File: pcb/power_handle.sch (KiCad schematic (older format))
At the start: 51 parts, among them J1 PJ-202A, J2 USB_C_Receptacle_USB2.0, Q1 PSMN6R0-25YLB, Q2 PSMN6R0-25YLB, Q3 BSS214NW, SW1 SW_SPST, U1 MCP73831T-2ATI/OT, U2 PAM2423, U3 BQ29703DSET

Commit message: pcb: Cleanup BOM items (#7)
Replaced out of stock components with substitutes
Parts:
- C10: Digikey 493-3094-1-ND -> 493-13738-1-ND
- D2, D4: Digikey B340LA-FDICT-ND -> 641-1258-1-ND
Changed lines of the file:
@@
 F 1 "B340LA-13-F" H 6200 3724 50  0000 C CNN
 F 2 "Diode_SMD:D_SMA" H 6200 3675 50  0001 C CNN
-F 3 "https://www.diodes.com/assets/Datasheets/ds30240.pdf" H 6200 3850 50  0001 C CNN
-F 4 "B340LA-FDICT-ND" H 6200 3850 50  0001 C CNN "Digikey"
+F 3 "https://www.comchiptech.com/admin/files/product/CDBA340L-HF%20RevC514368.pdf" H 6200 3850 50  0001 C CNN
+F 4 "641-1258-1-ND" H 6200 3850 50  0001 C CNN "Digikey"
 	1    6200 3850
 	-1   0    0    1
@@
 F 1 "B340LA-13-F" H 10450 2724 50  0000 C CNN
 F 2 "Diode_SMD:D_SMA" H 10450 2675 50  0001 C CNN
-F 3 "https://www.diodes.com/assets/Datasheets/ds30240.pdf" H 10450 2850 50  0001 C CNN
-F 4 "B340LA-FDICT-ND" H 10450 2850 50  0001 C CNN "Digikey"
+F 3 "https://www.comchiptech.com/admin/files/product/CDBA340L-HF%20RevC514368.pdf" H 10450 2850 50  0001 C CNN
+F 4 "641-1258-1-ND" H 10450 2850 50  0001 C CNN "Digikey"
 	1    10450 2850
 	-1   0    0    1
@@
 F 1 "1000u" H 7715 3955 50  0000 L CNN
 F 2 "Capacitor_SMD:CP_Elec_10x12.6" H 7600 4000 50  0001 C CNN
-F 3 "https://www.nichicon.co.jp/english/products/pdfs/e-pcg.pdf" H 7600 4000 50  0001 C CNN
-F 4 "493-3094-1-ND" H 7600 4000 50  0001 C CNN "Digikey"
+F 3 "https://www.nichicon.co.jp/english/products/pdfs/e-pcr.pdf" H 7600 4000 50  0001 C CNN
+F 4 "493-13738-1-ND" H 7600 4000 50  0001 C CNN "Digikey"
 	1    7600 4000
 	1    0    0    -1

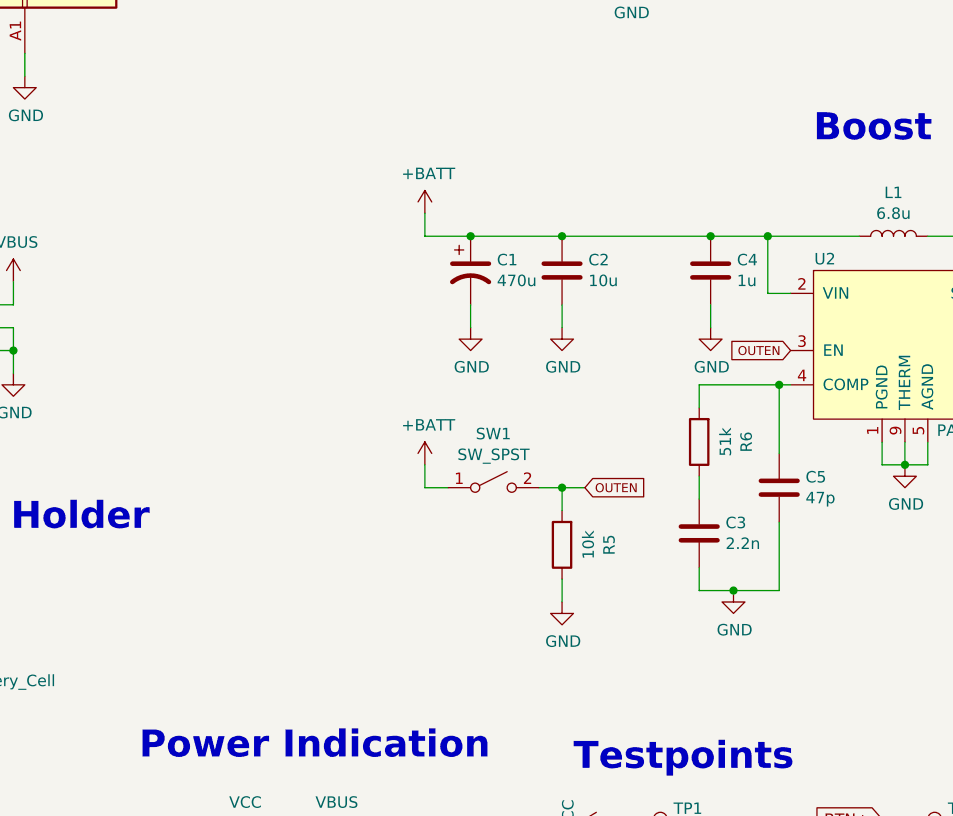
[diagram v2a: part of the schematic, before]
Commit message: pcb: implement improvements described in rev 1 bringup notes (#23)
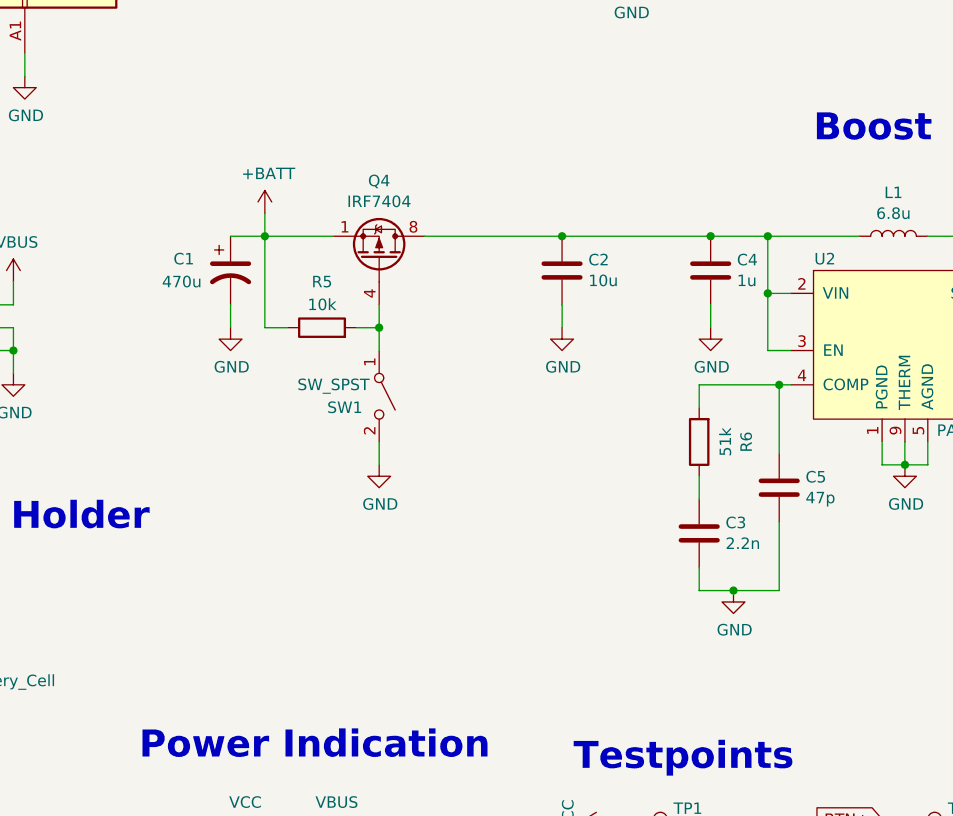
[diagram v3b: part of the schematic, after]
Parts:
- added Q4: IRF7404, Package_SO:SOIC-8_3.9x4.9mm_P1.27mm, symbol Transistor_FET:IRF7404
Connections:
- net +BATT: now also R5.1, Q4.1 (S), Q4.2 (S), Q4.3 (S); no longer C2.2, C4.2, L1.1, SW1.1 (A), U2.2 (VIN)
- net GND: now also SW1.2 (B); no longer R5.1
- removed net OUTEN: R5.2, SW1.2 (B), U2.3 (EN)
- new net: C2.2, C4.2, L1.1, Q4.5 (D), Q4.6 (D), Q4.7 (D), Q4.8 (D), U2.2 (VIN), U2.3 (EN)
- new net: Q4.4 (G), R5.2, SW1.1 (A)
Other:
- moved on the sheet: C1, R5, SW1
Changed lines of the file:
@@
 Connection ~ 6750 3850
-Wire Wire Line
-	3300 3750 3300 3850
-Wire Wire Line
-	3300 3850 3500 3850
-Wire Wire Line
-	3900 3850 3500 3850
-Connection ~ 3500 3850
 Wire Wire Line
 	3900 3850 4550 3850
@@
 Connection ~ 3900 3850
 Wire Wire Line
-	3500 4250 3500 4150
-Wire Wire Line
 	3900 4250 3900 4150
 Connection ~ 4550 3850
@@
 Wire Wire Line
 	4550 4250 4550 4150
-Text GLabel 4900 4350 0    39   Input ~ 0
-OUTEN
-Text GLabel 4000 4950 2    39   Input ~ 0
-OUTEN
-Wire Wire Line
-	4000 4950 3900 4950
-Wire Wire Line
-	3900 4950 3900 5050
-Wire Wire Line
-	3900 5350 3900 5450
-Wire Wire Line
-	3800 4950 3900 4950
-Connection ~ 3900 4950
-Wire Wire Line
-	3300 4850 3300 4950
-Wire Wire Line
-	3300 4950 3400 4950
+Wire Wire Line
+	3100 4750 3100 4850
 Wire Wire Line
 	4500 4900 4500 5000
@@
 $EndComp
 $Comp
-L power:+BATT #PWR012
-U 1 1 61903928
-P 3300 4850
-F 0 "#PWR012" H 3300 4700 50  0001 C CNN
-F 1 "+BATT" H 3315 5023 50  0000 C CNN
-F 2 "" H 3300 4850 50  0001 C CNN
-F 3 "" H 3300 4850 50  0001 C CNN
-	1    3300 4850
-	1    0    0    -1
-$EndComp
-$Comp
 L Switch:SW_SPST SW1
 U 1 1 6190069F
-P 3600 4950
-F 0 "SW1" H 3600 5185 50  0000 C CNN
-F 1 "SW_SPST" H 3600 5094 50  0000 C CNN
-F 2 "Button_Switch_THT:SW_E-Switch_EG1224_SPDT_Angled" H 3600 4950 50  0001 C CNN
-F 3 "https://sten-eswitch-13110800-production.s3.amazonaws.com/system/asset/product_line/data_sheet/119/EG.pdf" H 3600 4950 50  0001 C CNN
-F 4 "EG2585-ND" H 3600 4950 50  0001 C CNN "Digikey"
-	1    3600 4950
-	1    0    0    -1
+P 3100 4550
+F 0 "SW1" V 3150 4400 50  0000 C CNN
+F 1 "SW_SPST" V 3050 4350 50  0000 C CNN
+F 2 "Button_Switch_THT:SW_E-Switch_EG1224_SPDT_Angled" H 3100 4550 50  0001 C CNN
+F 3 "https://sten-eswitch-13110800-production.s3.amazonaws.com/system/asset/product_line/data_sheet/119/EG.pdf" H 3100 4550 50  0001 C CNN
+F 4 "EG2585-ND" H 3100 4550 50  0001 C CNN "Digikey"
+	1    3100 4550
+	0    1    1    0
 $EndComp
 $Comp
 L Device:R R5
 U 1 1 618EB047
-P 3900 5200
-F 0 "R5" V 3693 5200 50  0000 C CNN
-F 1 "10k" V 3784 5200 50  0000 C CNN
-F 2 "Resistor_SMD:R_0805_2012Metric" V 3830 5200 50  0001 C CNN
-F 3 "https://www.seielect.com/catalog/sei-rmcf_rmcp.pdf" H 3900 5200 50  0001 C CNN
-F 4 "RMCF0805JT10K0CT-ND" H 3900 5200 50  0001 C CNN "Digikey"
-	1    3900 5200
-	-1   0    0    1
+P 2850 4250
+F 0 "R5" V 3050 4250 50  0000 C CNN
+F 1 "10k" V 2950 4250 50  0000 C CNN
+F 2 "Resistor_SMD:R_0805_2012Metric" V 2780 4250 50  0001 C CNN
+F 3 "https://www.seielect.com/catalog/sei-rmcf_rmcp.pdf" H 2850 4250 50  0001 C CNN
+F 4 "RMCF0805JT10K0CT-ND" H 2850 4250 50  0001 C CNN "Digikey"
+	1    2850 4250
+	0    -1   -1   0
 $EndComp
 $Comp
 L power:GND #PWR015
 U 1 1 618EBB3E
-P 3900 5450
-F 0 "#PWR015" H 3900 5200 50  0001 C CNN
-F 1 "GND" H 3905 5277 50  0000 C CNN
-F 2 "" H 3900 5450 50  0001 C CNN
-F 3 "" H 3900 5450 50  0001 C CNN
-	1    3900 5450
+P 3100 4850
+F 0 "#PWR015" H 3100 4600 50  0001 C CNN
+F 1 "GND" H 3105 4677 50  0000 C CNN
+F 2 "" H 3100 4850 50  0001 C CNN
+F 3 "" H 3100 4850 50  0001 C CNN
+	1    3100 4850
 	1    0    0    -1
 $EndComp
@@
 $EndComp
 $Comp
-L power:GND #PWR013
-U 1 1 618D7836
-P 3500 4250
-F 0 "#PWR013" H 3500 4000 50  0001 C CNN
-F 1 "GND" H 3505 4077 50  0000 C CNN
-F 2 "" H 3500 4250 50  0001 C CNN
-F 3 "" H 3500 4250 50  0001 C CNN
-	1    3500 4250
-	1    0    0    -1
-$EndComp
-$Comp
-L Device:CP1 C1
-U 1 1 618D1D49
-P 3500 4000
-F 0 "C1" H 3615 4046 50  0000 L CNN
-F 1 "470u" H 3615 3955 50  0000 L CNN
-F 2 "Capacitor_SMD:CP_Elec_8x10" H 3500 4000 50  0001 C CNN
-F 3 "https://www.we-online.com/katalog/datasheet/875115252003.pdf" H 3500 4000 50  0001 C CNN
-F 4 "732-6451-1-ND" H 3500 4000 50  0001 C CNN "Digikey"
-	1    3500 4000
-	1    0    0    -1
-$EndComp
-$Comp
 L Device:C C2
 U 1 1 618D143D
@@
 L power:+BATT #PWR011
 U 1 1 618C9FC8
-P 3300 3750
-F 0 "#PWR011" H 3300 3600 50  0001 C CNN
-F 1 "+BATT" H 3315 3923 50  0000 C CNN
-F 2 "" H 3300 3750 50  0001 C CNN
-F 3 "" H 3300 3750 50  0001 C CNN
-	1    3300 3750
+P 2600 3750
+F 0 "#PWR011" H 2600 3600 50  0001 C CNN
+F 1 "+BATT" H 2615 3923 50  0000 C CNN
+F 2 "" H 2600 3750 50  0001 C CNN
+F 3 "" H 2600 3750 50  0001 C CNN
+	1    2600 3750
 	1    0    0    -1
 $EndComp
@@
 Text Notes 10050 2450 0    118  ~ 24
 Bypass
+$Comp
+L Transistor_FET:IRF7404 Q4
+U 1 1 61CC99EE
+P 3100 3950
+F 0 "Q4" V 3442 3950 50  0000 C CNN
+F 1 "IRF7404" V 3351 3950 50  0000 C CNN
+F 2 "Package_SO:SOIC-8_3.9x4.9mm_P1.27mm" H 3300 3875 50  0001 L CIN
+F 3 "http://www.infineon.com/dgdl/irf7404.pdf?fileId=5546d462533600a4015355fa2b5b1b9e" V 3100 3950 50  0001 L CNN
+F 4 "IRF7404PBFCT-ND" H 3100 3950 50  0001 C CNN "Digikey"
+	1    3100 3950
+	0    1    -1   0
+$EndComp
+Wire Wire Line
+	4900 4350 4800 4350
+Wire Wire Line
+	4800 4350 4800 4100
+Connection ~ 4800 4100
+Wire Wire Line
+	3000 4250 3100 4250
+Wire Wire Line
+	3100 4250 3100 4150
+Wire Wire Line
+	2700 4250 2600 4250
+Wire Wire Line
+	2600 3750 2600 3850
+Connection ~ 2600 3850
+Wire Wire Line
+	2600 3850 2600 4250
+Wire Wire Line
+	2600 3850 2900 3850
+Wire Wire Line
+	3100 4350 3100 4250
+Connection ~ 3100 4250
+$Comp
+L Device:CP1 C1
+U 1 1 618D1D49
+P 2450 4000
+F 0 "C1" H 2200 4050 50  0000 L CNN
+F 1 "470u" H 2150 3950 50  0000 L CNN
+F 2 "Capacitor_SMD:CP_Elec_8x10" H 2450 4000 50  0001 C CNN
+F 3 "https://www.we-online.com/katalog/datasheet/875115252003.pdf" H 2450 4000 50  0001 C CNN
+F 4 "732-6451-1-ND" H 2450 4000 50  0001 C CNN "Digikey"
+	1    2450 4000
+	1    0    0    -1
+$EndComp
+$Comp
+L power:GND #PWR013
+U 1 1 618D7836
+P 2450 4250
+F 0 "#PWR013" H 2450 4000 50  0001 C CNN
+F 1 "GND" H 2455 4077 50  0000 C CNN
+F 2 "" H 2450 4250 50  0001 C CNN
+F 3 "" H 2450 4250 50  0001 C CNN
+	1    2450 4250
+	1    0    0    -1
+$EndComp
+Wire Wire Line
+	2450 4250 2450 4150
+Wire Wire Line
+	3300 3850 3900 3850
+Wire Wire Line
+	2600 3850 2450 3850
 $EndSCHEMATC

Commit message: Revert "pcb: implement improvements described in rev 1 bringup notes (#23)"
This reverts commit 01e55846632a9cef383a24172751afed95ee1909.
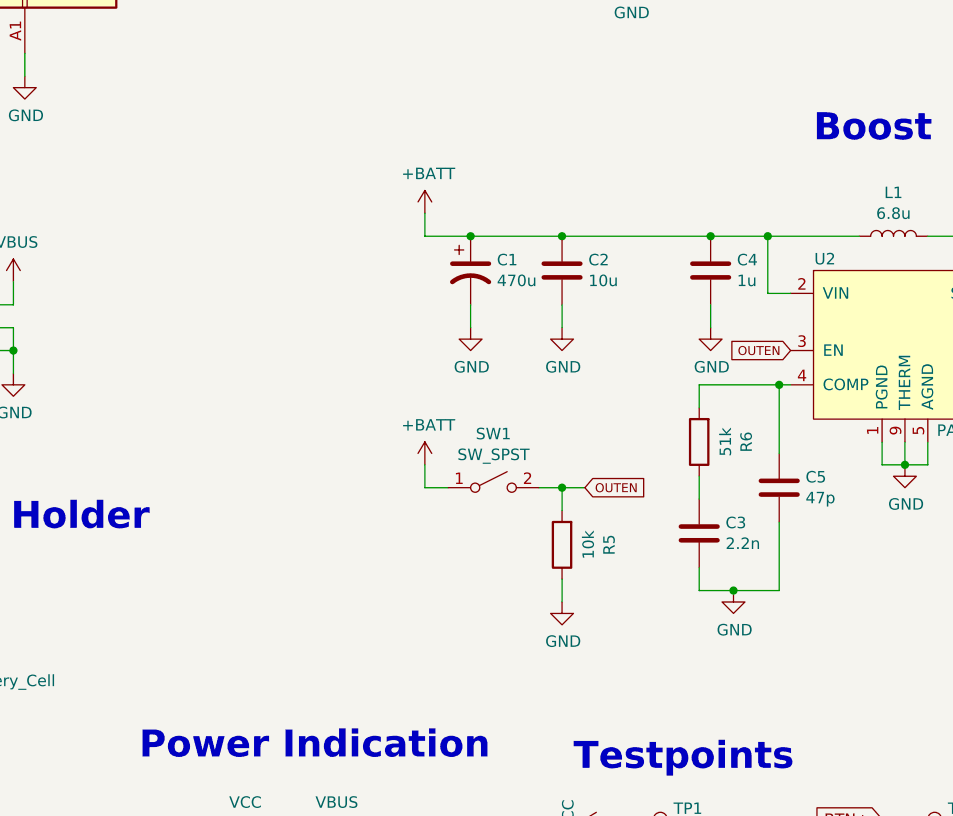
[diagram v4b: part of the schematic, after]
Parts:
- removed Q4: IRF7404, Package_SO:SOIC-8_3.9x4.9mm_P1.27mm, symbol Transistor_FET:IRF7404
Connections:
- net +BATT: now also C2.2, C4.2, L1.1, SW1.1 (A), U2.2 (VIN); no longer R5.1
- net GND: now also R5.1; no longer SW1.2 (B)
- net OUTEN: now reaches R5.2
- net OUTEN: now also SW1.2 (B), U2.3 (EN); no longer SW1.1 (A)
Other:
- moved on the sheet: C1, R5, SW1
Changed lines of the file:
@@
 Connection ~ 6750 3850
+Wire Wire Line
+	3300 3750 3300 3850
+Wire Wire Line
+	3300 3850 3500 3850
+Wire Wire Line
+	3900 3850 3500 3850
+Connection ~ 3500 3850
 Wire Wire Line
 	3900 3850 4550 3850
@@
 Connection ~ 3900 3850
 Wire Wire Line
+	3500 4250 3500 4150
+Wire Wire Line
 	3900 4250 3900 4150
 Connection ~ 4550 3850
@@
 Wire Wire Line
 	4550 4250 4550 4150
-Wire Wire Line
-	3100 4750 3100 4850
+Text GLabel 4900 4350 0    39   Input ~ 0
+OUTEN
+Text GLabel 4000 4950 2    39   Input ~ 0
+OUTEN
+Wire Wire Line
+	4000 4950 3900 4950
+Wire Wire Line
+	3900 4950 3900 5050
+Wire Wire Line
+	3900 5350 3900 5450
+Wire Wire Line
+	3800 4950 3900 4950
+Connection ~ 3900 4950
+Wire Wire Line
+	3300 4850 3300 4950
+Wire Wire Line
+	3300 4950 3400 4950
 Wire Wire Line
 	4500 4900 4500 5000
@@
 $EndComp
 $Comp
+L power:+BATT #PWR012
+U 1 1 61903928
+P 3300 4850
+F 0 "#PWR012" H 3300 4700 50  0001 C CNN
+F 1 "+BATT" H 3315 5023 50  0000 C CNN
+F 2 "" H 3300 4850 50  0001 C CNN
+F 3 "" H 3300 4850 50  0001 C CNN
+	1    3300 4850
+	1    0    0    -1
+$EndComp
+$Comp
 L Switch:SW_SPST SW1
 U 1 1 6190069F
-P 3100 4550
-F 0 "SW1" V 3150 4400 50  0000 C CNN
-F 1 "SW_SPST" V 3050 4350 50  0000 C CNN
-F 2 "Button_Switch_THT:SW_E-Switch_EG1224_SPDT_Angled" H 3100 4550 50  0001 C CNN
-F 3 "https://sten-eswitch-13110800-production.s3.amazonaws.com/system/asset/product_line/data_sheet/119/EG.pdf" H 3100 4550 50  0001 C CNN
-F 4 "EG2585-ND" H 3100 4550 50  0001 C CNN "Digikey"
-	1    3100 4550
-	0    1    1    0
+P 3600 4950
+F 0 "SW1" H 3600 5185 50  0000 C CNN
+F 1 "SW_SPST" H 3600 5094 50  0000 C CNN
+F 2 "Button_Switch_THT:SW_E-Switch_EG1224_SPDT_Angled" H 3600 4950 50  0001 C CNN
+F 3 "https://sten-eswitch-13110800-production.s3.amazonaws.com/system/asset/product_line/data_sheet/119/EG.pdf" H 3600 4950 50  0001 C CNN
+F 4 "EG2585-ND" H 3600 4950 50  0001 C CNN "Digikey"
+	1    3600 4950
+	1    0    0    -1
 $EndComp
 $Comp
 L Device:R R5
 U 1 1 618EB047
-P 2850 4250
-F 0 "R5" V 3050 4250 50  0000 C CNN
-F 1 "10k" V 2950 4250 50  0000 C CNN
-F 2 "Resistor_SMD:R_0805_2012Metric" V 2780 4250 50  0001 C CNN
-F 3 "https://www.seielect.com/catalog/sei-rmcf_rmcp.pdf" H 2850 4250 50  0001 C CNN
-F 4 "RMCF0805JT10K0CT-ND" H 2850 4250 50  0001 C CNN "Digikey"
-	1    2850 4250
-	0    -1   -1   0
+P 3900 5200
+F 0 "R5" V 3693 5200 50  0000 C CNN
+F 1 "10k" V 3784 5200 50  0000 C CNN
+F 2 "Resistor_SMD:R_0805_2012Metric" V 3830 5200 50  0001 C CNN
+F 3 "https://www.seielect.com/catalog/sei-rmcf_rmcp.pdf" H 3900 5200 50  0001 C CNN
+F 4 "RMCF0805JT10K0CT-ND" H 3900 5200 50  0001 C CNN "Digikey"
+	1    3900 5200
+	-1   0    0    1
 $EndComp
 $Comp
 L power:GND #PWR015
 U 1 1 618EBB3E
-P 3100 4850
-F 0 "#PWR015" H 3100 4600 50  0001 C CNN
-F 1 "GND" H 3105 4677 50  0000 C CNN
-F 2 "" H 3100 4850 50  0001 C CNN
-F 3 "" H 3100 4850 50  0001 C CNN
-	1    3100 4850
+P 3900 5450
+F 0 "#PWR015" H 3900 5200 50  0001 C CNN
+F 1 "GND" H 3905 5277 50  0000 C CNN
+F 2 "" H 3900 5450 50  0001 C CNN
+F 3 "" H 3900 5450 50  0001 C CNN
+	1    3900 5450
 	1    0    0    -1
 $EndComp
@@
 $EndComp
 $Comp
+L power:GND #PWR013
+U 1 1 618D7836
+P 3500 4250
+F 0 "#PWR013" H 3500 4000 50  0001 C CNN
+F 1 "GND" H 3505 4077 50  0000 C CNN
+F 2 "" H 3500 4250 50  0001 C CNN
+F 3 "" H 3500 4250 50  0001 C CNN
+	1    3500 4250
+	1    0    0    -1
+$EndComp
+$Comp
+L Device:CP1 C1
+U 1 1 618D1D49
+P 3500 4000
+F 0 "C1" H 3615 4046 50  0000 L CNN
+F 1 "470u" H 3615 3955 50  0000 L CNN
+F 2 "Capacitor_SMD:CP_Elec_8x10" H 3500 4000 50  0001 C CNN
+F 3 "https://www.we-online.com/katalog/datasheet/875115252003.pdf" H 3500 4000 50  0001 C CNN
+F 4 "732-6451-1-ND" H 3500 4000 50  0001 C CNN "Digikey"
+	1    3500 4000
+	1    0    0    -1
+$EndComp
+$Comp
 L Device:C C2
 U 1 1 618D143D
@@
 L power:+BATT #PWR011
 U 1 1 618C9FC8
-P 2600 3750
-F 0 "#PWR011" H 2600 3600 50  0001 C CNN
-F 1 "+BATT" H 2615 3923 50  0000 C CNN
-F 2 "" H 2600 3750 50  0001 C CNN
-F 3 "" H 2600 3750 50  0001 C CNN
-	1    2600 3750
+P 3300 3750
+F 0 "#PWR011" H 3300 3600 50  0001 C CNN
+F 1 "+BATT" H 3315 3923 50  0000 C CNN
+F 2 "" H 3300 3750 50  0001 C CNN
+F 3 "" H 3300 3750 50  0001 C CNN
+	1    3300 3750
 	1    0    0    -1
 $EndComp
@@
 Text Notes 10050 2450 0    118  ~ 24
 Bypass
-$Comp
-L Transistor_FET:IRF7404 Q4
-U 1 1 61CC99EE
-P 3100 3950
-F 0 "Q4" V 3442 3950 50  0000 C CNN
-F 1 "IRF7404" V 3351 3950 50  0000 C CNN
-F 2 "Package_SO:SOIC-8_3.9x4.9mm_P1.27mm" H 3300 3875 50  0001 L CIN
-F 3 "http://www.infineon.com/dgdl/irf7404.pdf?fileId=5546d462533600a4015355fa2b5b1b9e" V 3100 3950 50  0001 L CNN
-F 4 "IRF7404PBFCT-ND" H 3100 3950 50  0001 C CNN "Digikey"
-	1    3100 3950
-	0    1    -1   0
-$EndComp
-Wire Wire Line
-	4900 4350 4800 4350
-Wire Wire Line
-	4800 4350 4800 4100
-Connection ~ 4800 4100
-Wire Wire Line
-	3000 4250 3100 4250
-Wire Wire Line
-	3100 4250 3100 4150
-Wire Wire Line
-	2700 4250 2600 4250
-Wire Wire Line
-	2600 3750 2600 3850
-Connection ~ 2600 3850
-Wire Wire Line
-	2600 3850 2600 4250
-Wire Wire Line
-	2600 3850 2900 3850
-Wire Wire Line
-	3100 4350 3100 4250
-Connection ~ 3100 4250
-$Comp
-L Device:CP1 C1
-U 1 1 618D1D49
-P 2450 4000
-F 0 "C1" H 2200 4050 50  0000 L CNN
-F 1 "470u" H 2150 3950 50  0000 L CNN
-F 2 "Capacitor_SMD:CP_Elec_8x10" H 2450 4000 50  0001 C CNN
-F 3 "https://www.we-online.com/katalog/datasheet/875115252003.pdf" H 2450 4000 50  0001 C CNN
-F 4 "732-6451-1-ND" H 2450 4000 50  0001 C CNN "Digikey"
-	1    2450 4000
-	1    0    0    -1
-$EndComp
-$Comp
-L power:GND #PWR013
-U 1 1 618D7836
-P 2450 4250
-F 0 "#PWR013" H 2450 4000 50  0001 C CNN
-F 1 "GND" H 2455 4077 50  0000 C CNN
-F 2 "" H 2450 4250 50  0001 C CNN
-F 3 "" H 2450 4250 50  0001 C CNN
-	1    2450 4250
-	1    0    0    -1
-$EndComp
-Wire Wire Line
-	2450 4250 2450 4150
-Wire Wire Line
-	3300 3850 3900 3850
-Wire Wire Line
-	2600 3850 2450 3850
 $EndSCHEMATC
